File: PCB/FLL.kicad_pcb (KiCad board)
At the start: 2 copper layers, 16 parts, among them U2 MCP73831-2-OT, U3 LM317L_SOT-89

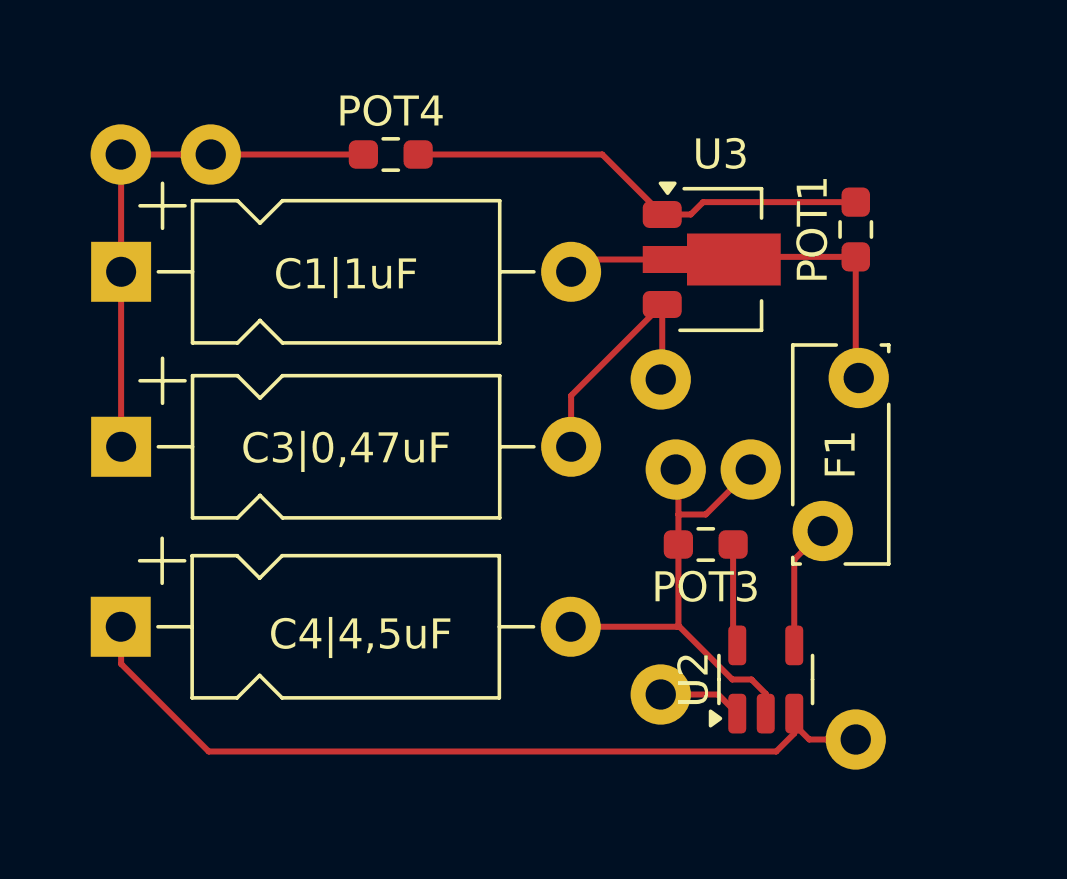
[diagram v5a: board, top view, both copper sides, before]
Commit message: Update PCB design configuration and remove unnecessary files
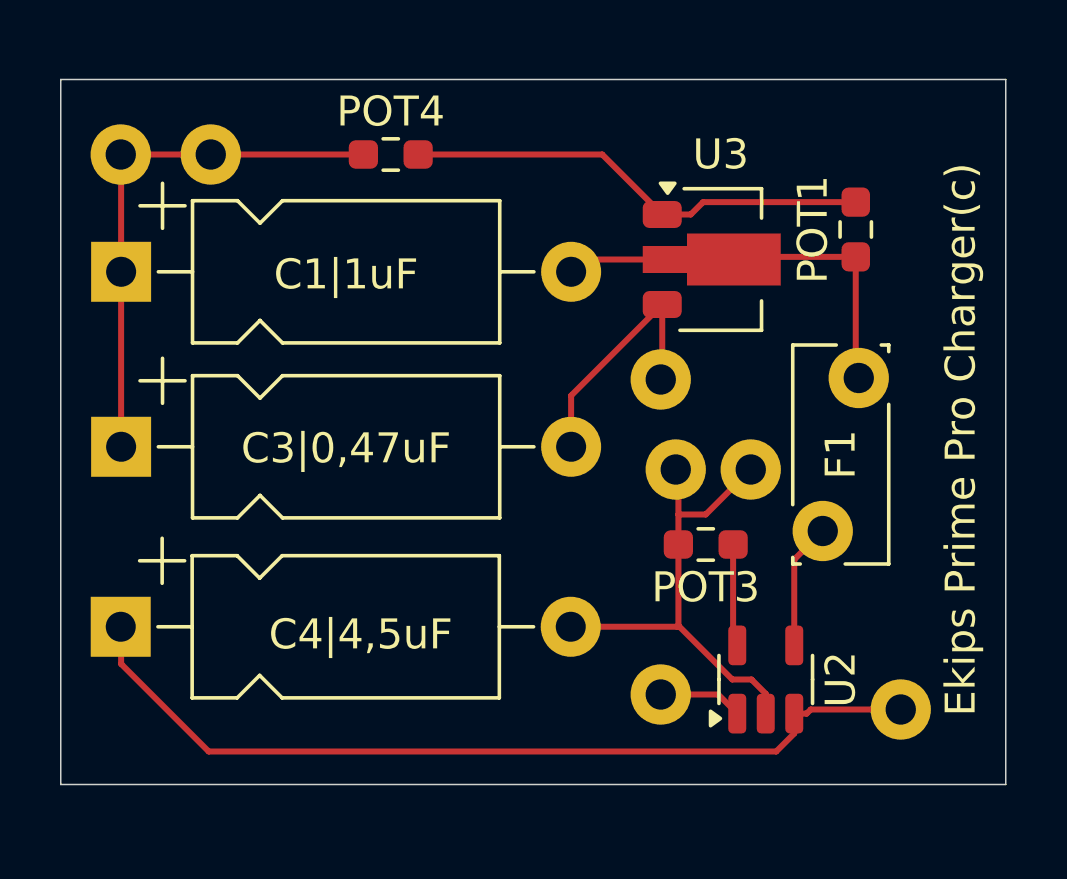
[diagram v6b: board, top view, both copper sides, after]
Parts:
- moved ? 1.80 mm to (158.0, 52.5)
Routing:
- net +7.5V: track 28.4 -> 29.8 mm
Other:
- board outline added: 31.5 x 23.5 mm
- board text added: "Ekips Prime Pro Charger(c)"
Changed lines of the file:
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@@
 		(tags "resistor handsolder")
 		(property "Reference" "POT3"
-			(at 0 -1.43 360)
+			(at 0 -1.43 0)
 			(layer "F.SilkS")
 			(effects
@@
 		)
 		(property "Value" "1kΩ"
-			(at 0 1.43 360)
+			(at 0 1.43 0)
 			(layer "F.Fab")
 			(effects
@@
 		)
 		(fp_text user "${REFERENCE}"
-			(at 0 0 360)
+			(at 0 0 0)
 			(layer "F.Fab")
 			(effects
@@
 		(tags "SOT TO_SOT_SMD")
 		(property "Reference" "U2"
-			(at 0 -2.4 90)
+			(at 0 2.5 90)
 			(layer "F.SilkS")
 			(effects
@@
 	(footprint ""
 		(layer "F.Cu")
-		(at 156.5 53.5)
+		(at 158 52.5)
 		(property "Reference" ""
 			(at 0 0 0)
@@
 		)
 	)
+	(gr_line
+		(start 130 31.5)
+		(end 161.5 31.5)
+		(stroke
+			(width 0.05)
+			(type default)
+		)
+		(layer "Edge.Cuts")
+	)
+	(gr_line
+		(start 130 55)
+		(end 130 31.5)
+		(stroke
+			(width 0.05)
+			(type default)
+		)
+		(layer "Edge.Cuts")
+	)
+	(gr_line
+		(start 161.5 31.5)
+		(end 161.5 55)
+		(stroke
+			(width 0.05)
+			(type default)
+		)
+		(layer "Edge.Cuts")
+	)
+	(gr_line
+		(start 161.5 55)
+		(end 130 55)
+		(stroke
+			(width 0.05)
+			(type default)
+		)
+		(layer "Edge.Cuts")
+	)
+	(gr_text "Ekips Prime Pro Charger(c)"
+		(at 160 43.5 90)
+		(layer "F.SilkS")
+		(effects
+			(font
+				(size 1 1)
+				(thickness 0.15)
+			)
+		)
+	)
 	(segment
-		(start 154.45 53)
-		(end 154.95 53.5)
+		(start 154.8625 52.6375)
+		(end 155 52.5)
+		(width 0.2)
+		(layer "F.Cu")
+		(net 1)
+	)
+	(segment
+		(start 155 52.5)
+		(end 158 52.5)
 		(width 0.2)
 		(layer "F.Cu")
@@
 	)
 	(segment
-		(start 154.95 53.5)
-		(end 156.5 53.5)
+		(start 154.45 53.299999)
+		(end 153.849999 53.9)
 		(width 0.2)
 		(layer "F.Cu")
@@
 	)
 	(segment
-		(start 154.45 53.299999)
-		(end 153.849999 53.9)
+		(start 154.45 52.6375)
+		(end 154.8625 52.6375)
 		(width 0.2)
 		(layer "F.Cu")

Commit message: Added Mouser Electronics Parts
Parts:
- added C**: C1210, C1210C475K4PACTU_(4.7 uF):C1210, F.Cu at (63.0, 17.0)
- added C**: C0805, C0805C474K5RACTU_(0.47 uF):C0805, F.Cu at (52.4, 31.0)
- added C**: C0805, C0805C105K4RACTU_(1 uF):C0805, F.Cu at (52.4, 24.5)
- added F**: 1206L05015YR, 1206L075THYR_(290 mOhms):1206L05015YR, F.Cu at (53.0, 17.0)
- added IC**: SOT95P270X145-5N, MCP73831T-2ACI/OT:SOT95P270X145-5N, F.Cu at (62.8, 33.0)
- added R**: RESC1608X55N, RC0603FR-071KL_(1 kOhms):RESC1608X55N, F.Cu at (62.8, 28.0)
- added R**: ERJ2RKD1004X, ERJ-2RHD1401X_(1.4 kOhms):ERJ2RKD1004X, F.Cu at (63.0, 23.0)
- moved ? 116.2 mm to (20.0, 17.5)
- moved ? 116.2 mm to (38.0, 28.0)
- moved ? 116.2 mm to (35.5, 28.0)
- moved ? 116.2 mm to (35.0, 25.0)
- moved ? 116.2 mm to (17.0, 17.5)
- moved ? 116.2 mm to (35.0, 35.5)
- moved ? 116.2 mm to (43.0, 36.0)
- moved C4|4,5uF 116.2 mm to (17.0, 33.2)
- moved POT1 116.2 mm to (41.5, 20.0)
- moved POT3 116.2 mm to (36.5, 30.5)
- moved POT4 116.2 mm to (26.0, 17.5)
- moved U2 116.2 mm to (38.5, 35.0)
- moved U3 116.2 mm to (37.0, 21.0)
- moved C1|1uF 116.2 mm to (17.0, 21.4)
- moved C3|0,47uF 116.2 mm to (17.0, 27.2)
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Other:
- outline, holes or cut-outs redrawn
- board text added: "+12V"
- board text added: "+7.5V"
- board text added: "-V"
- board text added: "0.47uF"
- board text added: "1.4kOhms"
- board text added: "1kOhms"
- board text added: "1uF"
- board text added: "290mOhms"
- board text added: "4.7uF"
- board text added: "Ekips Prime Pro Charger © 2024"
- board text added: "GND"
- board text added: "MCP73831T-2ACI/OT"
- board text added: "STAT"
- board text removed: "Ekips Prime Pro Charger(c)"

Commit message: chore: Remove unused KiCad symbol files
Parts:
- removed C**: C1210, C1210C475K4PACTU_(4.7 uF):C1210
- removed C**: C0805, C0805C474K5RACTU_(0.47 uF):C0805
- removed C**: C0805, C0805C105K4RACTU_(1 uF):C0805
- removed F**: 1206L05015YR, 1206L075THYR_(290 mOhms):1206L05015YR
- removed IC**: SOT95P270X145-5N, MCP73831T-2ACI/OT:SOT95P270X145-5N
- removed R**: RESC1608X55N, RC0603FR-071KL_(1 kOhms):RESC1608X55N
- removed R**: ERJ2RKD1004X, ERJ-2RHD1401X_(1.4 kOhms):ERJ2RKD1004X
- C3: renamed from C3|0,47uF; footprint Capacitor_THT:CP_Axial_L10.0mm_D4.5mm_P15.00mm_Horizontal -> C0805C474K5RACTU:C0805
- C4: renamed from C4|4,5uF; value 4,5uF -> 4,7uF; footprint Capacitor_THT:CP_Axial_L10.0mm_D4.5mm_P15.00mm_Horizontal -> C1210C475K4PACTU:C1210
- C4: renamed from C1|1uF; footprint Capacitor_THT:CP_Axial_L10.0mm_D4.5mm_P15.00mm_Horizontal -> C0805C105K4RACTU:C0805
- POT1: value 240Ω -> 1206L05015YR; footprint Resistor_SMD:R_0603_1608Metric_Pad0.98x0.95mm_HandSolder -> 1206L075THYR:1206L05015YR
- POT3, POT4: footprint Resistor_SMD:R_0603_1608Metric_Pad0.98x0.95mm_HandSolder -> ERJ-2RHD1401X:ERJ2RKD1004X
- moved POT3 13.1 mm to (23.4, 31.6)
- moved ? 12.6 mm to (25.4, 28.1)
- moved ? 12.6 mm to (22.9, 28.1)
- moved ? 12.6 mm to (22.4, 25.1)
- moved ? 12.6 mm to (22.4, 35.5)
- moved ? 12.6 mm to (30.4, 36.0)
- moved F1 12.6 mm to (29.0, 25.0)
- moved POT1 12.6 mm to (28.9, 20.1)
- moved U2 12.6 mm to (25.9, 35.0)
- moved U3 12.6 mm to (24.4, 21.1)
- moved ? 10.6 mm to (19.4, 28.1)
- moved ? 10.6 mm to (16.9, 28.1)
- moved POT4 8.08 mm to (17.9, 17.6)
- moved C3 2.84 mm to (17.9, 24.6)
- moved C4 1.23 mm to (17.9, 34.0), turned to 90 degrees
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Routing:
- net +7.5V: track 29.8 -> 14.6 mm
- net GND: track 17.9 -> 13.8 mm
- net Net-(U3-ADJ): track 15.6 -> 11.5 mm
- net -7.5V: track 16.4 -> 18.9 mm
- net Net-(U3-VI): track 8.52 -> 7.02 mm
- net Net-(U2-PROG): track 3.42 -> 2.79 mm
- net Net-(U3-VO): track 13.8 -> 14.3 mm
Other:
- board size 31.5 x 23.5 mm -> 18.4 x 23.5 mm
- board text removed: "0.47uF"
- board text removed: "1.4kOhms"
- board text removed: "1kOhms"
- board text removed: "1uF"
- board text removed: "290mOhms"
- board text removed: "4.7uF"
- board text removed: "MCP73831T-2ACI/OT"
